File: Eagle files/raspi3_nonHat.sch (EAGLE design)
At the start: 1 part, among them K1 PIN20X2

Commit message: eagle up
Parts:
- added A1: (no value), CEDT_JANUARY_2015_v5:AUDIO-JACKPTH
- added C13, C15, C17: 1uf, rcl:C-EUC1206
- added C14: 470uF, resistor:CPOL-EUE5-10.5
- added C16: 0.1uf, rcl:C-EUC1206
- added C30: (no value), CEDT_SEPTEMBER_V2:CAP_POL_10V
- added C4, C5, C6: (no value), adafruit:C-USC0603K
- added EN2: PEC11L-4220F-S0015, Encoders:PEC11L-4220F-S0015
- added IC5: PAM8403, PAM8403:PAM8403
- added LED1: LED3MM, CEDT_JANUARY_2015_v5:LED3MM
- added OLED_MODULE: DIY-MODULES_DISPLAY-OLED-128X64-I2C, esp32_dev_kit_v14:DIY-MODULES_DISPLAY-OLED-128X64-I2C
- added R1, R2, R3: 10k, CEDT:RESISTOR0207/7
- added R6, R7, R8: (no value), rcl:R-US_M0805
- added SL2: (no value), con-amp-quick:M05
- added SPEAKER: (no value), CEDT_JANUARY_2015_v5:M02
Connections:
- new net C16: C16.2
- new net CLK: C4.1, EN2.B, R6.1, SL2.1
- new net DT: C5.1, EN2.A, R7.1, SL2.2
- new net N$1: LED1.A, R3.2
- new net N$27: IC5.-OUT_R, SPEAKER.2
- new net N$29: A1.LEFT, IC5.INR
- new net N$34: C16.1, IC5.VREF
- new net N$4: IC5.+OUT_R, SPEAKER.1
- new net SCL: OLED_MODULE.SCL, R1.1
- new net SDA: OLED_MODULE.SDA, R2.1
- new net SW: C6.1, EN2.1, R8.2, SL2.3
- net +3V3: now also OLED_MODULE.VCC, R1.2, R2.2
- net +5V: now also C13.1, C14.+, C15.2, C17.2, C30.+, IC5.MUTE, IC5.PVDD, IC5.PVDD1, IC5.SHND, IC5.VDD, R3.1, R6.2, R7.2, R8.1, SL2.5
- net GND: now also A1.SLEEVE, C13.2, C14.-, C15.1, C17.1, C30.-, C4.2, C5.2, C6.2, EN2.2, EN2.C, IC5.GND, IC5.NC, IC5.PGND, IC5.PGND1, LED1.C, OLED_MODULE.GND, SL2.4
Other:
- note added: "Audio Amplifier"

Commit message: 30-eagle2
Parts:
- removed SL2: (no value), con-amp-quick:M05
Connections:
- removed net C16: C16.2
- net +5V: no longer SL2.5
- net CLK: no longer SL2.1
- net DT: no longer SL2.2
- net GND: now also C16.2; no longer SL2.4
- net SW: no longer SL2.3
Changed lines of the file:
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@@
 <?xml version="1.0" encoding="utf-8"?>
 <!DOCTYPE eagle SYSTEM "eagle.dtd">
-<eagle version="9.4.1">
+<eagle version="9.6.2">
 <drawing>
 <settings>
@@
 <part name="GND19" library="MSP PROJECT LIBRARY" deviceset="GND" device=""/>
 <part name="C16" library="rcl" deviceset="C-EU" device="C1206" value="0.1uf"/>
-<part name="GND22" library="MSP PROJECT LIBRARY" deviceset="GND" device=""/>
 <part name="C13" library="rcl" deviceset="C-EU" device="C1206" value="1uf"/>
 <part name="GND25" library="MSP PROJECT LIBRARY" deviceset="GND" device=""/>
@@
 <part name="R7" library="rcl" library_urn="urn:adsk.eagle:library:334" deviceset="R-US_" device="M0805" package3d_urn="urn:adsk.eagle:package:23556/2"/>
 <part name="R8" library="rcl" library_urn="urn:adsk.eagle:library:334" deviceset="R-US_" device="M0805" package3d_urn="urn:adsk.eagle:package:23556/2"/>
-<part name="SL2" library="con-amp-quick" library_urn="urn:adsk.eagle:library:125" deviceset="M05" device="" package3d_urn="urn:adsk.eagle:package:5961/1"/>
 <part name="GND8" library="Arduino_Hackathon_v5" deviceset="GND" device=""/>
 <part name="GND11" library="Arduino_Hackathon_v5" deviceset="GND" device=""/>
 <part name="GND12" library="Arduino_Hackathon_v5" deviceset="GND" device=""/>
-<part name="GND13" library="Arduino_Hackathon_v5" deviceset="GND" device=""/>
 <part name="P+2" library="supply1" deviceset="+5V" device=""/>
-<part name="P+4" library="supply1" deviceset="+5V" device=""/>
 <part name="P+6" library="supply1" deviceset="+5V" device=""/>
 <part name="LED1" library="CEDT_JANUARY_2015_v5" deviceset="LED" device="3MM"/>
@@
 <part name="GND2" library="MSP PROJECT LIBRARY" deviceset="GND" device=""/>
 <part name="P+7" library="supply1" deviceset="+5V" device=""/>
+<part name="GND5" library="MSP PROJECT LIBRARY" deviceset="GND" device=""/>
 </parts>
 <sheets>
@@
 <attribute name="NAME" x="-36.449" y="42.545" size="1.778" layer="95"/>
 </instance>
-<instance part="GND22" gate="1" x="-36.83" y="38.1" smashed="yes">
-<attribute name="VALUE" x="-39.37" y="35.56" size="1.778" layer="96"/>
-</instance>
 <instance part="C13" gate="G$1" x="-66.04" y="57.15" smashed="yes">
 <attribute name="NAME" x="-65.659" y="52.705" size="1.778" layer="95"/>
@@
 <attribute name="VALUE" x="-39.37" y="100.838" size="1.778" layer="96"/>
 </instance>
-<instance part="SL2" gate="G$1" x="10.16" y="109.22" smashed="yes">
-<attribute name="VALUE" x="7.62" y="99.06" size="1.778" layer="96"/>
-<attribute name="NAME" x="7.62" y="117.602" size="1.778" layer="95"/>
-</instance>
 <instance part="GND8" gate="1" x="-3.81" y="99.06" smashed="yes">
 <attribute name="VALUE" x="-6.35" y="96.52" size="1.778" layer="96"/>
@@
 <attribute name="VALUE" x="-58.42" y="100.33" size="1.778" layer="96"/>
 </instance>
-<instance part="GND13" gate="1" x="27.94" y="109.22" smashed="yes">
-<attribute name="VALUE" x="25.4" y="106.68" size="1.778" layer="96"/>
-</instance>
 <instance part="P+2" gate="1" x="-3.81" y="128.27" smashed="yes">
 <attribute name="VALUE" x="-2.54" y="130.81" size="1.778" layer="96" rot="R180"/>
-</instance>
-<instance part="P+4" gate="1" x="27.94" y="118.11" smashed="yes">
-<attribute name="VALUE" x="29.21" y="120.65" size="1.778" layer="96" rot="R180"/>
 </instance>
 <instance part="P+6" gate="1" x="-40.64" y="110.49" smashed="yes">
@@
 <instance part="P+7" gate="1" x="-63.5" y="96.52" smashed="yes">
 <attribute name="VALUE" x="-62.23" y="99.06" size="1.778" layer="96" rot="R180"/>
+</instance>
+<instance part="GND5" gate="1" x="-36.83" y="38.1" smashed="yes">
+<attribute name="VALUE" x="-39.37" y="35.56" size="1.778" layer="96"/>
 </instance>
 </instances>
@@
 </segment>
 <segment>
-<pinref part="SL2" gate="G$1" pin="4"/>
-<pinref part="GND13" gate="1" pin="GND"/>
-<wire x1="17.78" y1="111.76" x2="27.94" y2="111.76" width="0.1524" layer="91"/>
-</segment>
-<segment>
 <pinref part="LED1" gate="G$1" pin="C"/>
 <wire x1="-63.5" y1="72.39" x2="-63.5" y2="69.85" width="0.1524" layer="91"/>
 <pinref part="GND2" gate="1" pin="GND"/>
+</segment>
+<segment>
+<pinref part="C16" gate="G$1" pin="2"/>
+<wire x1="-36.83" y1="41.91" x2="-36.83" y2="40.64" width="0.1524" layer="91"/>
+<pinref part="GND5" gate="1" pin="GND"/>
 </segment>
 </net>
@@
 </segment>
 <segment>
-<pinref part="SL2" gate="G$1" pin="5"/>
-<wire x1="17.78" y1="114.3" x2="27.94" y2="114.3" width="0.1524" layer="91"/>
-<pinref part="P+4" gate="1" pin="+5V"/>
-<wire x1="27.94" y1="115.57" x2="27.94" y2="114.3" width="0.1524" layer="91"/>
-</segment>
-<segment>
 <pinref part="R3" gate="G$1" pin="1"/>
 <wire x1="-63.5" y1="91.44" x2="-63.5" y2="93.98" width="0.1524" layer="91"/>
@@
 <wire x1="-35.56" y1="50.8" x2="-36.83" y2="50.8" width="0.1524" layer="91"/>
 <wire x1="-36.83" y1="50.8" x2="-36.83" y2="49.53" width="0.1524" layer="91"/>
-</segment>
-</net>
-<net name="C16" class="0">
-<segment>
-<pinref part="C16" gate="G$1" pin="2"/>
-<pinref part="GND22" gate="1" pin="GND"/>
-<wire x1="-36.83" y1="41.91" x2="-36.83" y2="40.64" width="0.1524" layer="91"/>
 </segment>
 </net>
@@
 <label x="-57.15" y="120.65" size="1.778" layer="95"/>
 </segment>
-<segment>
-<pinref part="SL2" gate="G$1" pin="2"/>
-<wire x1="21.59" y1="106.68" x2="17.78" y2="106.68" width="0.1524" layer="91"/>
-<label x="21.59" y="106.045" size="1.778" layer="95"/>
-</segment>
 </net>
 <net name="CLK" class="0">
@@
 <label x="-66.04" y="120.65" size="1.778" layer="95"/>
 </segment>
-<segment>
-<pinref part="SL2" gate="G$1" pin="1"/>
-<wire x1="21.59" y1="104.14" x2="17.78" y2="104.14" width="0.1524" layer="91"/>
-<label x="21.59" y="103.505" size="1.778" layer="95"/>
-</segment>
 </net>
 <net name="SW" class="0">
@@
 <label x="-49.53" y="120.65" size="1.778" layer="95"/>
 </segment>
-<segment>
-<pinref part="SL2" gate="G$1" pin="3"/>
-<wire x1="21.59" y1="109.22" x2="17.78" y2="109.22" width="0.1524" layer="91"/>
-<label x="21.59" y="108.585" size="1.778" layer="95"/>
-</segment>
-</net>
+</net>

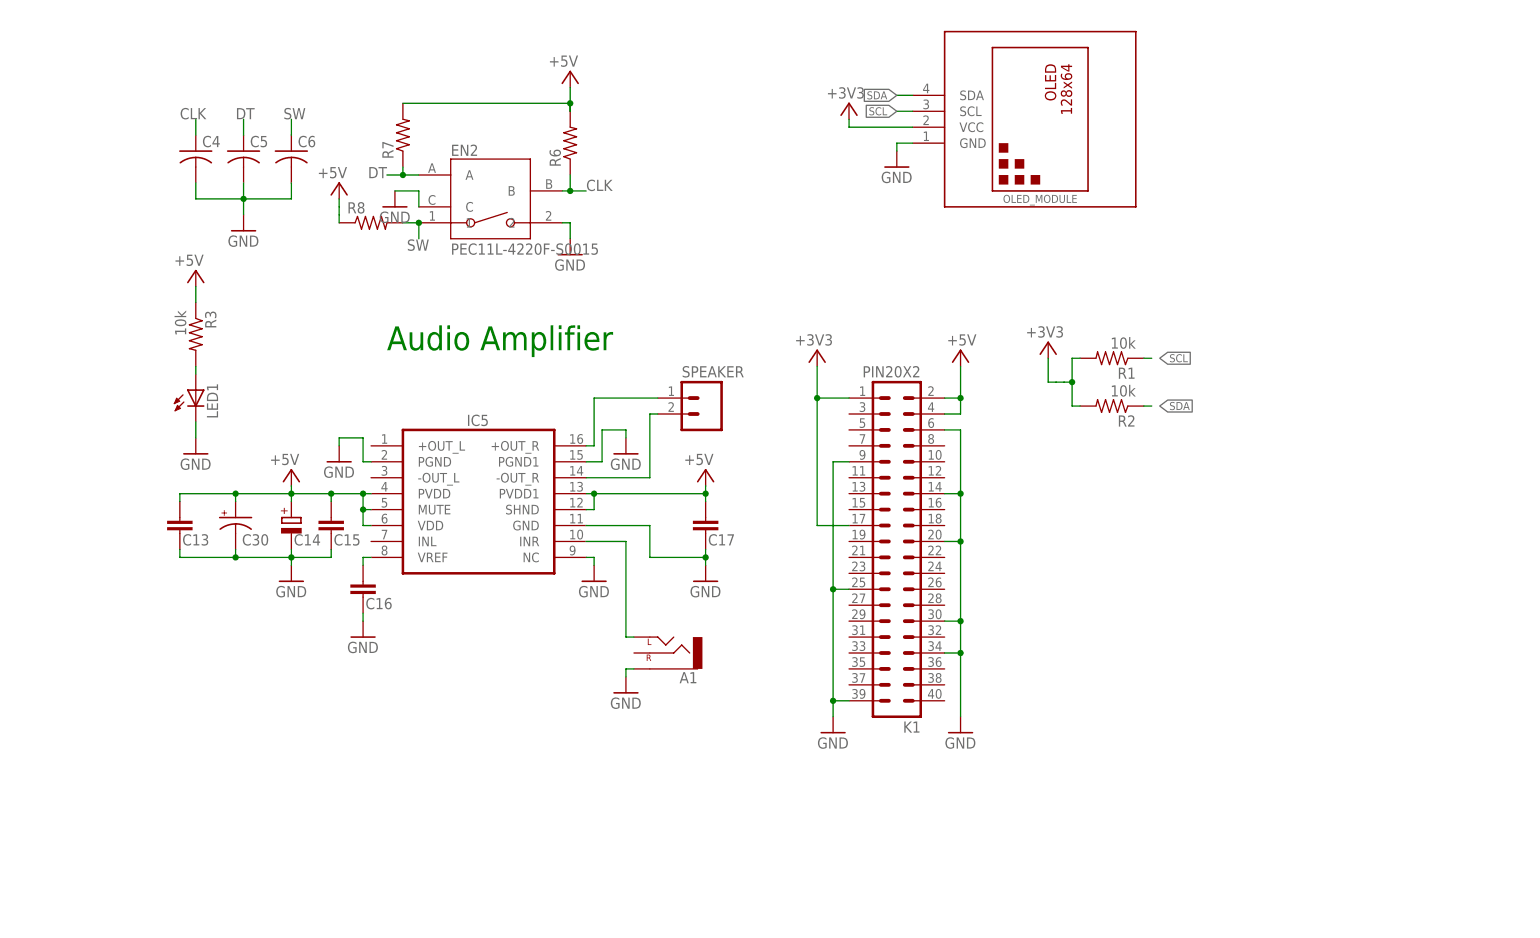
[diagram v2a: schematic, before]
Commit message: added ads1115
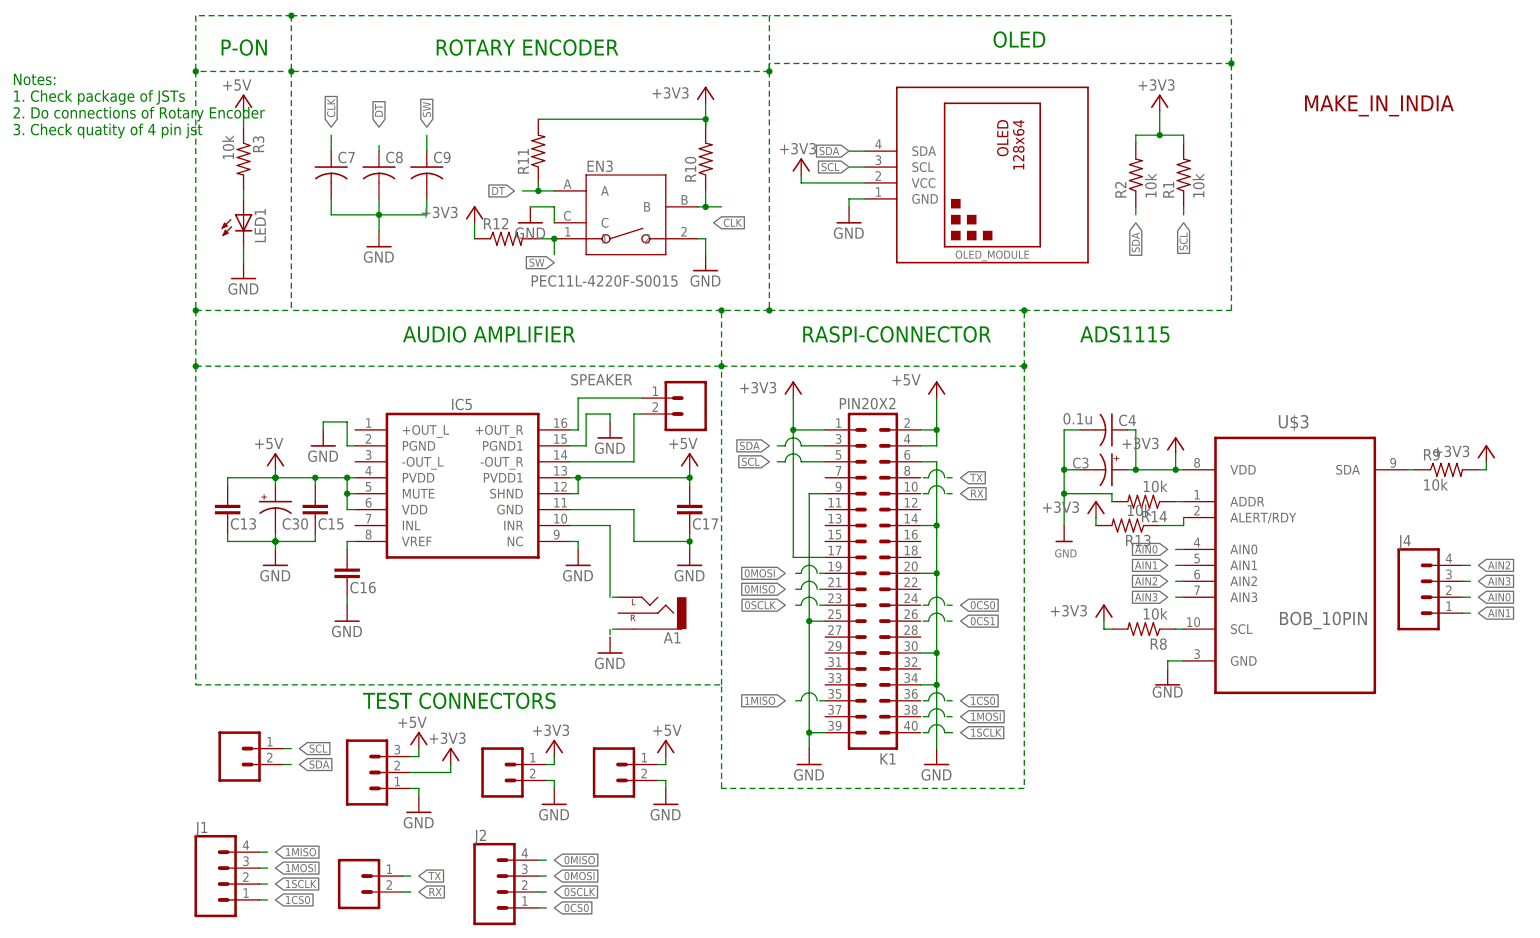
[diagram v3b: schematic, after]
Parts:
- removed C14: 470uF, resistor:CPOL-EUE5-10.5
- removed C5, C6: (no value), adafruit:C-USC0603K
- removed EN2: PEC11L-4220F-S0015, Encoders:PEC11L-4220F-S0015
- removed R6, R7: (no value), rcl:R-US_M0805
- added C3: 10u, CEDT_JANUARY_2015_v5:CAP_POL_10V
- added C7, C8, C9: (no value), adafruit:C-USC0603K
- added EN3: PEC11L-4220F-S0015, Encoders:PEC11L-4220F-S0015
- added J1, J2, J4: (no value), SparkFun-Connectors:CONN_04POLAR
- added POWER: (no value), SparkFun-Connectors:CONN_03POLAR
- added R10, R11, R12: (no value), rcl:R-US_M0805
- added R13, R14, R9: 10k, CEDT_JANUARY_2015_v5:RESISTOR0603
- added THERMISTOR1, THERMISTOR2, THERMISTOR3, THERMISTOR4: (no value), SparkFun-Connectors:CONN_02POLAR
- added U$1: MAKE-IN-INDIA-LOGO, namanpuri:MAKE-IN-INDIA-LOGO
- added U$3: BOB_10PIN, CEDT_JANUARY_2015_v5:BOB_10PIN
- C4: value (none) -> 0.1u; device adafruit:C-USC0603K -> CEDT_JANUARY_2015_v5:CAP0805
- R8: value (none) -> 10k; device rcl:R-US_M0805 -> CEDT_JANUARY_2015_v5:RESISTOR0603
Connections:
- new net 0CS0: J2.1, K1.24
- new net 0CS1: K1.26
- new net 0MISO: J2.4, K1.21
- new net 0MOSI: J2.3, K1.19
- new net 0SCLK: J2.2, K1.23
- new net 1CS0: J1.1, K1.36
- new net 1MISO: J1.4, K1.35
- new net 1MOSI: J1.3, K1.38
- new net 1SCLK: J1.2, K1.40
- new net AIN0: J4.2, U$3.AIN0
- new net AIN1: J4.1, U$3.AIN1
- new net AIN2: J4.4, U$3.AIN2
- new net AIN3: J4.3, U$3.AIN3
- new net N$12: R8.1, U$3.SCL
- new net N$13: R9.1, U$3.SDA
- new net N$14: R13.1, U$3.ALERT/RDY
- new net N$15: R14.1, U$3.ADDR
- new net RX: K1.10, THERMISTOR4.2
- new net TX: K1.8, THERMISTOR4.1
- net +3V3: now also C3.+, C4.1, POWER.2, R10.2, R11.2, R12.1, R13.2, R8.2, R9.2, THERMISTOR2.1, U$3.VDD
- net +5V: now also POWER.3, THERMISTOR3.1; no longer C14.+, R6.2, R7.2, R8.1
- net CLK: now also C7.1, EN3.B, R10.1; no longer C4.1, EN2.B, R6.1
- net DT: now also C8.1, EN3.A, R11.1; no longer C5.1, EN2.A, R7.1
- net GND: now also C3.-, C7.2, C8.2, C9.2, EN3.2, EN3.C, POWER.1, R14.2, THERMISTOR2.2, THERMISTOR3.2, U$3.GND; no longer C14.-, C5.2, C6.2, EN2.2, EN2.C
- net SCL: now also K1.5, THERMISTOR1.1
- net SDA: now also K1.3, THERMISTOR1.2
- net SW: now also C9.1, EN3.1, R12.2; no longer C6.1, EN2.1, R8.2
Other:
- note added: "ADS1115"
- note added: "AUDIO AMPLIFIER"
- note added: "Notes: 1. Check package of JSTs 2. Do connections of Rotary Encoder 3. Check quatity of 4 pin jst"
- note added: "OLED"
- note added: "P-ON"
- note added: "RASPI-CONNECTOR"
- note added: "ROTARY ENCODER"
- note added: "TEST CONNECTORS"
- note removed: "Audio Amplifier"
- moved on the sheet: A1, C13, C15, C16, C17, C30, C4, IC5, K1, LED1, OLED_MODULE, R1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
